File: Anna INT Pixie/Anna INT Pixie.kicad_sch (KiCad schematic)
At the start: 20 parts, among them J1 Conn_01x13_Pin, J2 Conn_01x02_Pin, J3 Conn_01x02_Pin, J4 Conn_01x01_Socket, J5 Conn_01x01_Socket, U1 MCP6002-xMC, U2 MCP6002-xMC

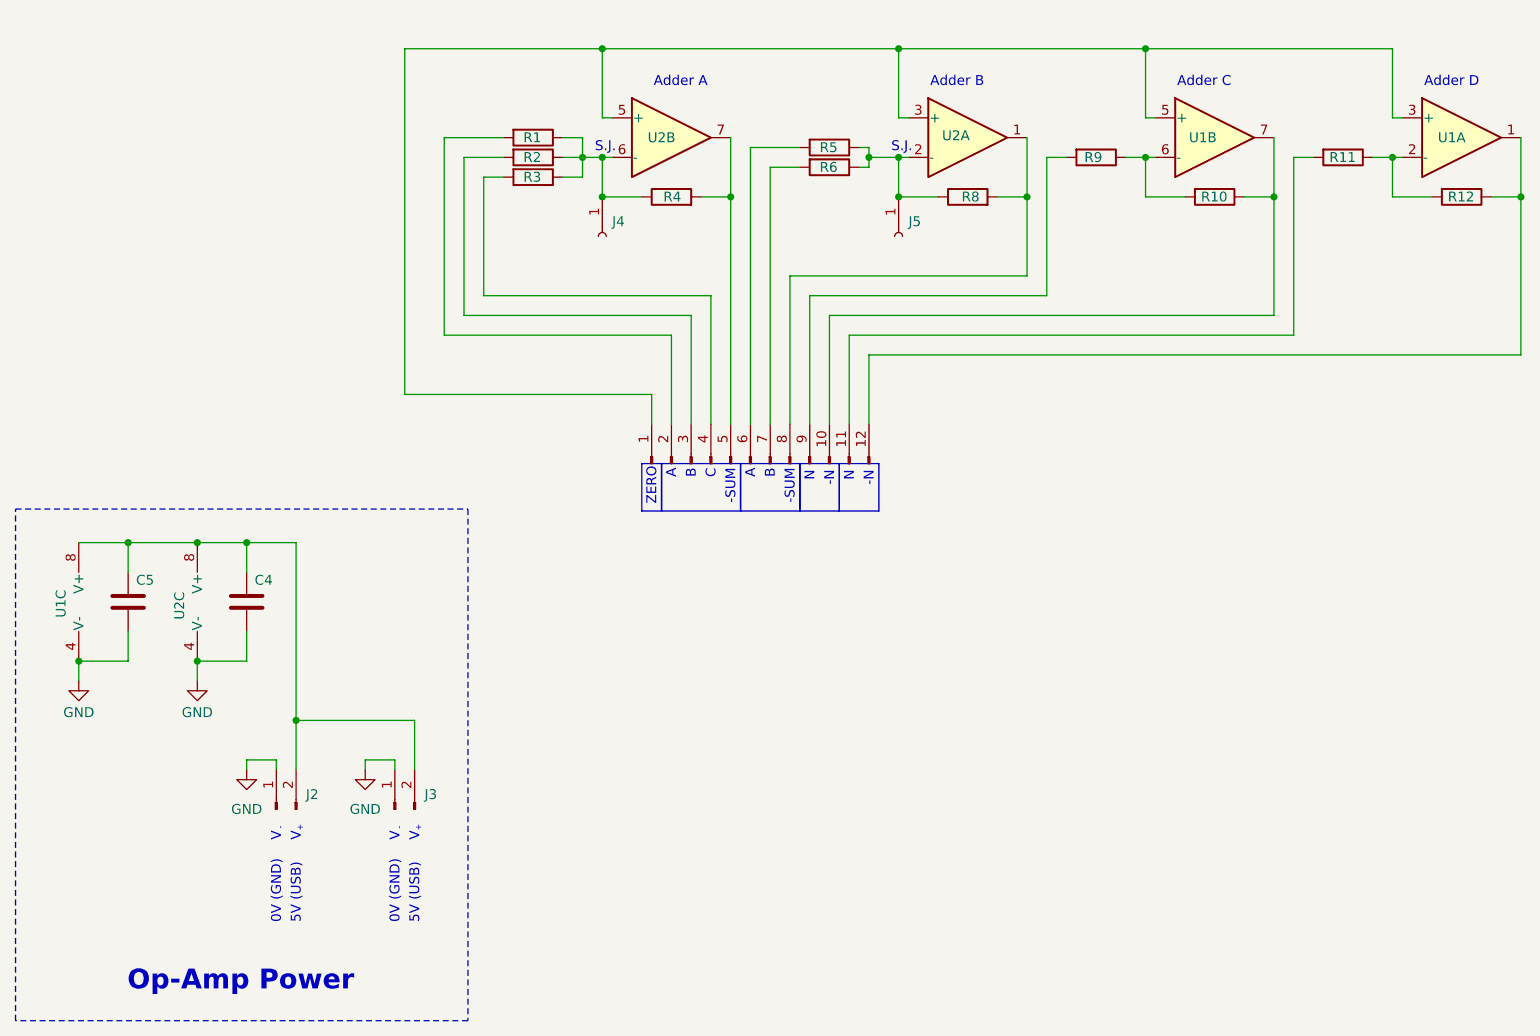
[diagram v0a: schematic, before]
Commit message: Added INT module. Also updated ADD module with larger SJ holes.
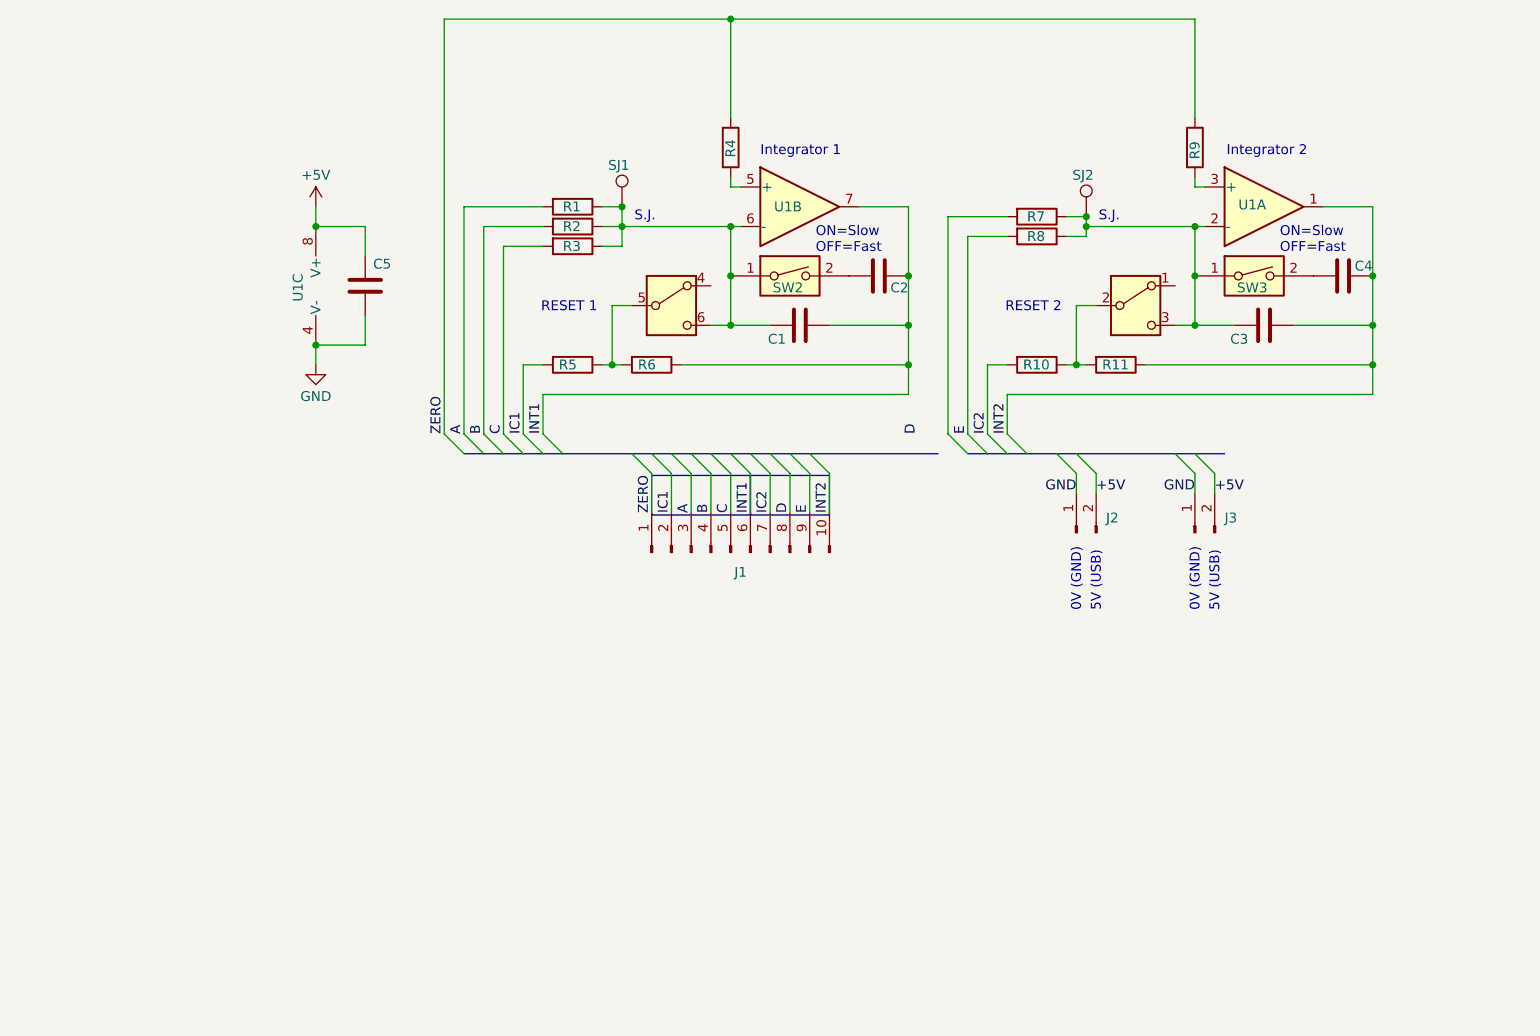
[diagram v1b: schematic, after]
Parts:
- removed J1: Conn_01x13_Pin, Connector_PinHeader_2.54mm:PinHeader_1x12_P2.54mm_Vertical, symbol Connector:Conn_01x12_Pin
- removed J4, J5: Conn_01x01_Socket, Connector_PinSocket_2.54mm:PinSocket_1x01_P2.54mm_Vertical, symbol Connector:Conn_01x01_Socket
- removed R12, R9: 100 kΩ, Resistor_SMD:R_1206_3216Metric, symbol Device:R
- removed U2: MCP6002-xMC, PCM_JLCPCB:SOIC-8_L4.9-W3.9-P1.27-LS6.0-BL, symbol Amplifier_Operational:MCP6002-xMC
- added C1, C3: 0.1 µF, Capacitor_THT:C_Rect_L7.0mm_W3.5mm_P2.50mm_P5.00mm, symbol Device:C
- added C2: 1 µF, Capacitor_THT:C_Rect_L7.0mm_W3.5mm_P2.50mm_P5.00mm, symbol Device:C
- added J1: Conn_01x10_Pin, Connector_PinHeader_2.54mm:PinHeader_1x10_P2.54mm_Vertical, symbol Connector:Conn_01x10_Pin
- added R5, R6: 100 kΩ, Resistor_SMD:R_1206_3216Metric, symbol Device:R
- added SJ1, SJ2: TestPoint, TestPoint:TestPoint_THTPad_2.0x2.0mm_Drill1.0mm, symbol Connector:TestPoint
- added SW1: SW_DPDT_x2, Button_Switch_THT:SW_Push_2P2T_Toggle_CK_PVA2xxH1xxxxxxV2, symbol Switch:SW_DPDT_x2
- added SW2, SW3: SW_DIP_x01, Button_Switch_THT:SW_DIP_SPSTx01_Piano_10.8x4.1mm_W7.62mm_P2.54mm, symbol Switch:SW_DIP_x01
- C4: value 0.1 µF -> 1 µF; footprint Capacitor_SMD:C_0805_2012Metric -> Capacitor_THT:C_Rect_L7.0mm_W3.5mm_P2.50mm_P5.00mm; LCSC C49678 -> (none); now left out of the parts list
- R1, R2, R3, R4: value 100 kΩ -> 1 MΩ; LCSC C17900 -> C17927
- R7: renamed from R5; value 100 kΩ -> 1 MΩ; LCSC C17900 -> C17927
- R8: renamed from R6; value 100 kΩ -> 1 MΩ; LCSC C17900 -> C17927
- R9: renamed from R8; value 100 kΩ -> 1 MΩ; LCSC C17900 -> C17927
- U1: footprint PCM_JLCPCB:SOIC-8_L4.9-W3.9-P1.27-LS6.0-BL -> Package_SO:SOIC-8_3.9x4.9mm_P1.27mm
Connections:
- net GND: no longer C4.2
- net +5V: now reaches C5.1, J2.2 (Pin_2), J3.2 (Pin_2), U1.8 (V+)
- net +5V: no longer C4.1
- net INT2: now reaches U1.1
- net INT2: now also C4.2, R11.1, C3.2, J1.10 (Pin_10)
- net at U1.2 (-): now also R7.1, R8.1, C3.1, SJ2.1, SW1.3 (C), SW3.1; no longer R11.1
- net at R10.1: now also R11.2, SW1.2 (B); no longer U1.7
- net at U1.6 (-): now also R1.1, R2.1, R3.1, C1.1, SJ1.1, SW1.6 (C), SW2.1; no longer R10.2
- net at R9.2: now also U1.3 (+)
- net at U1.5 (+): now also R4.2; no longer U1.3 (+)
- net E: now reaches R8.2
- net E: now also J1.9 (Pin_9)
- net C: now reaches R3.2
- net C: now also J1.5 (Pin_5)
- net B: now reaches R2.2
- net B: now also J1.4 (Pin_4)
- net A: now reaches R1.2
- net A: now also J1.3 (Pin_3)
- new net: C4.1, SW3.2
- new net: C2.1, SW2.2
- new net: R5.1, R6.2, SW1.5 (B)
- new net D: J1.8 (Pin_8)
- new net IC1: J1.2 (Pin_2), R5.2
- new net IC2: J1.7 (Pin_7), R10.2
- new net INT1: C1.2, C2.2, J1.6 (Pin_6), R6.1, U1.7
- new net ZERO: J1.1 (Pin_1), R4.1, R9.1
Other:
- note added: "Integrator 1"
- note added: "Integrator 2"
- note added: "ON=Slow OFF=Fast"
- note added: "RESET 1"
- note added: "RESET 2"
- note removed: "+"
- note removed: "-"
- note removed: "-N"
- note removed: "-SUM"
- note removed: "A"
- note removed: "Adder A"
- note removed: "Adder B"
- note removed: "Adder C"
- note removed: "Adder D"
- note removed: "B"
- note removed: "C"
- note removed: "N"
- note removed: "Op-Amp Power"
- note removed: "V"
- note removed: "ZERO"
- title: ADD Pixie (Anna) -> INT Pixie (Anna)
- moved on the sheet: C5, J2, J3, R1, R2, R3, R4, R7, R8, R9, U1A, U1C
